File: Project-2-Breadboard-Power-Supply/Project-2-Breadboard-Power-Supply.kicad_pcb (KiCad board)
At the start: 2 copper layers, 33.2 x 52.5 mm, 17 parts, among them J1 Conn_01x02_Pin, J2 Conn_01x02_Pin, J3 Conn_01x03_Pin, J4 Conn_01x03_Pin, J5 Screw_Terminal_01x02, J6 Barrel_Jack_Switch, J7 Screw_Terminal_01x02, U1 LM7805_TO220, U2 LM317_TO-220

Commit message: add GND plane
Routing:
- net GND: track 0.00 -> 35.0 mm
- added copper zone on B.Cu, net GND
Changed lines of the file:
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@@
 	)
 	(footprint "Custom_Library_0.pretty:SW_1218_EWI"
-		(locked yes)
 		(layer "F.Cu")
 		(at 47.1509 58.25 90)
 		(tags "EG1218 ")
 		(property "Reference" "S1"
-			(at 0 2.5 90)
+			(at -3.15 -1.7509 0)
 			(unlocked yes)
 			(layer "F.SilkS")
+			(hide yes)
 			(effects
 				(font
@@
 		)
 		(property "Value" "EG1218"
-			(at 0 2.5 90)
+			(at -3.15 2.9491 0)
 			(unlocked yes)
 			(layer "F.Fab")
@@
 			(layer "F.Fab")
 		)
-		(fp_text user "*"
-			(at -2.5019 0 90)
-			(layer "F.SilkS")
-			(effects
-				(font
-					(size 1 1)
-					(thickness 0.15)
-				)
-			)
-		)
-		(fp_text user "*"
-			(at -2.5019 0 90)
-			(unlocked yes)
-			(layer "F.SilkS")
-			(effects
-				(font
-					(size 1 1)
-					(thickness 0.15)
-				)
-			)
-		)
-		(fp_text user "*"
-			(at -1.6129 0 90)
-			(layer "F.Fab")
-			(effects
-				(font
-					(size 1 1)
-					(thickness 0.15)
-				)
-			)
-		)
-		(fp_text user "*"
-			(at -1.6129 0 90)
-			(unlocked yes)
-			(layer "F.Fab")
-			(effects
-				(font
-					(size 1 1)
-					(thickness 0.15)
-				)
-			)
-		)
 		(fp_text user "${REFERENCE}"
-			(at 0 2.5 90)
+			(at -3.15 -1.8509 0)
 			(unlocked yes)
 			(layer "F.Fab")
@@
 	)
 	(segment
+		(start 61 47.5)
+		(end 60.962 47.5)
+		(width 0.25)
+		(layer "B.Cu")
+		(net "GND")
+	)
+	(segment
+		(start 49.845 47.355)
+		(end 47.97 49.23)
+		(width 0.25)
+		(layer "B.Cu")
+		(net "GND")
+	)
+	(segment
+		(start 35.69 60.5)
+		(end 35.69 59.306)
+		(width 0.25)
+		(layer "B.Cu")
+		(net "GND")
+	)
+	(segment
+		(start 59.305 94.945)
+		(end 49.845 94.945)
+		(width 0.25)
+		(layer "B.Cu")
+		(net "GND")
+	)
+	(segment
+		(start 60.962 47.5)
+		(end 60.817 47.355)
+		(width 0.25)
+		(layer "B.Cu")
+		(net "GND")
+	)
+	(segment
+		(start 35.69 59.306)
+		(end 37.25 57.746)
+		(width 0.25)
+		(layer "B.Cu")
+		(net "GND")
+	)
+	(segment
+		(start 60.817 47.355)
+		(end 49.845 47.355)
+		(width 0.25)
+		(layer "B.Cu")
+		(net "GND")
+	)
+	(segment
+		(start 61 93.25)
+		(end 59.305 94.945)
+		(width 0.25)
+		(layer "B.Cu")
+		(net "GND")
+	)
+	(segment
+		(start 37.25 57.746)
+		(end 37.25 54.5)
+		(width 0.25)
+		(layer "B.Cu")
+		(net "GND")
+	)
+	(segment
+		(start 49.845 94.945)
+		(end 47.97 93.07)
+		(width 0.25)
+		(layer "B.Cu")
+		(net "GND")
+	)
+	(segment
 		(start 54.81 79.75)
 		(end 54.81 83.5)
@@
 		(net "Net-(D1-A)")
 	)
+	(zone
+		(net "GND")
+		(layer "B.Cu")
+		(hatch edge 0.5)
+		(connect_pads
+			(clearance 0.5)
+		)
+		(min_thickness 0.25)
+		(fill yes
+			(mode hatch)
+			(thermal_gap 0.5)
+			(thermal_bridge_width 0.5)
+			(island_removal_mode 0)
+			(hatch_thickness 1)
+			(hatch_gap 1.5)
+			(hatch_orientation 0)
+			(hatch_border_algorithm hatch_thickness)
+			(hatch_min_hole_area 0.15)
+		)
+		(polygon
+			(pts
+				(xy 30.75 45.5) (xy 30.25 46) (xy 30.25 97) (xy 30.75 97.5) (xy 62.5 97.5) (xy 63 97.1) (xy 63 91.75)
+				(xy 62.5 91.25) (xy 57 91.25) (xy 56 90.25) (xy 56 52.75) (xy 57 51.75) (xy 62.5 51.75) (xy 63 51.25)
+				(xy 63 46) (xy 62.55 45.5)
+			)
+		)
+	)
 	(embedded_fonts no)

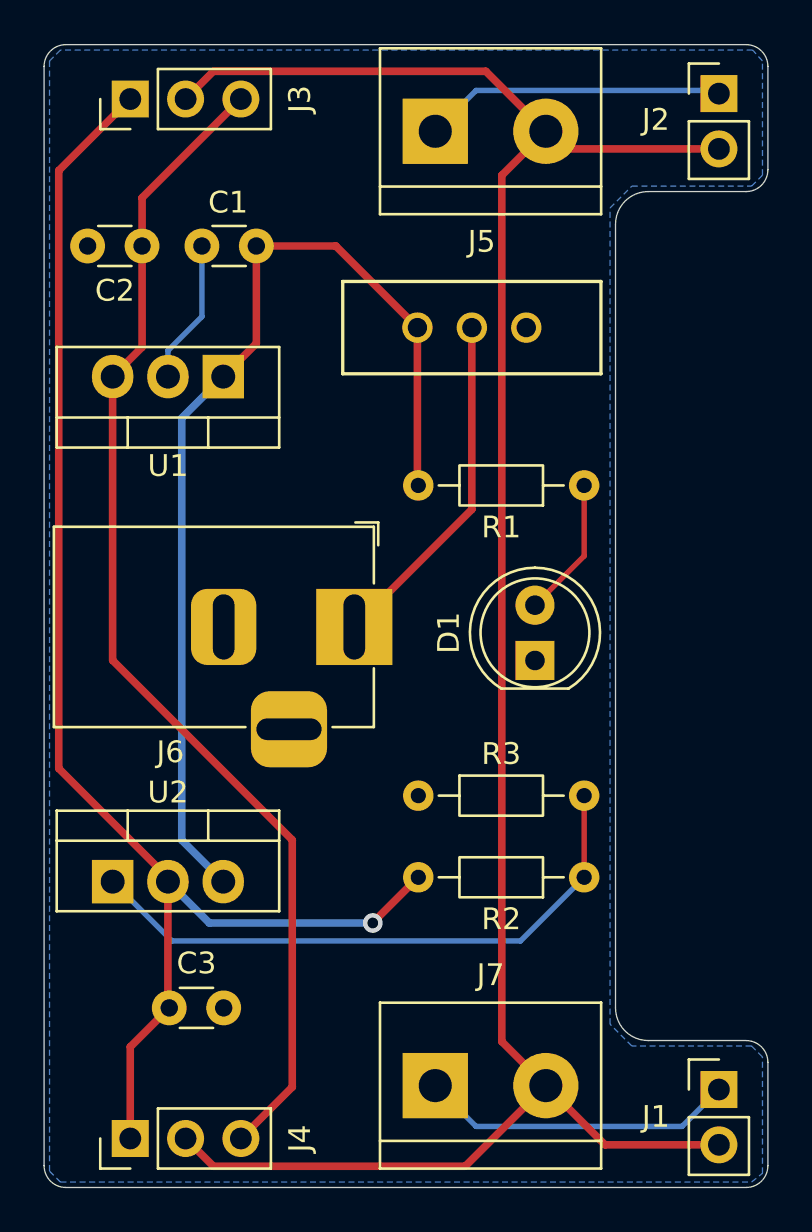
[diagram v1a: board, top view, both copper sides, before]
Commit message: add all Front Silkscreen designators and free text
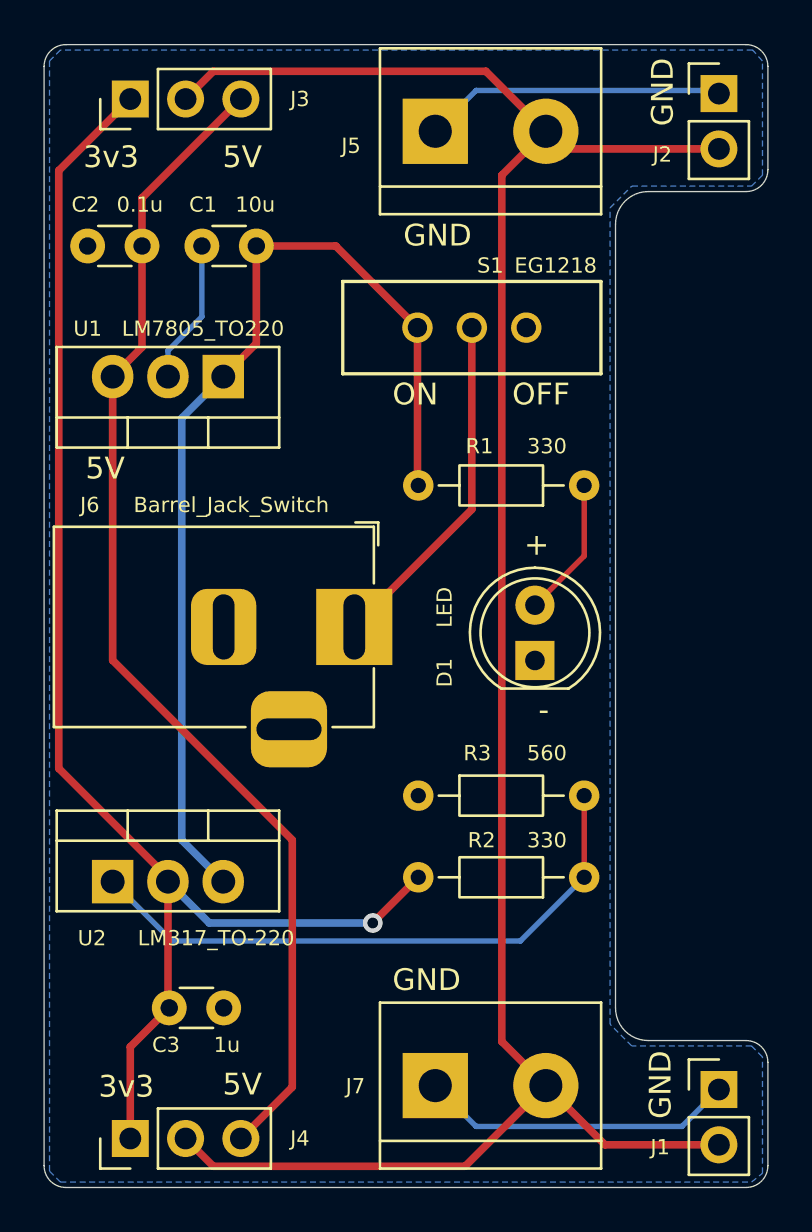
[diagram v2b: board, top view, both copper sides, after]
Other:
- board text added: "+"
- board text added: "-"
- board text added: "3v3"
- board text added: "5V"
- board text added: "GND"
- board text added: "OFF"
- board text added: "ON"

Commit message: add all front and back silkscreen footprints (logos and text like version info)
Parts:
- added REF**: KiCad-Logo2_5mm_SilkScreen, Symbol:KiCad-Logo2_5mm_SilkScreen, B.Cu at (52.0, 66.0)
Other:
- board text added: "Breadboard Power Supply"
- board text added: "version0.1"
